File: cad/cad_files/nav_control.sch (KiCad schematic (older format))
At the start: 10 parts

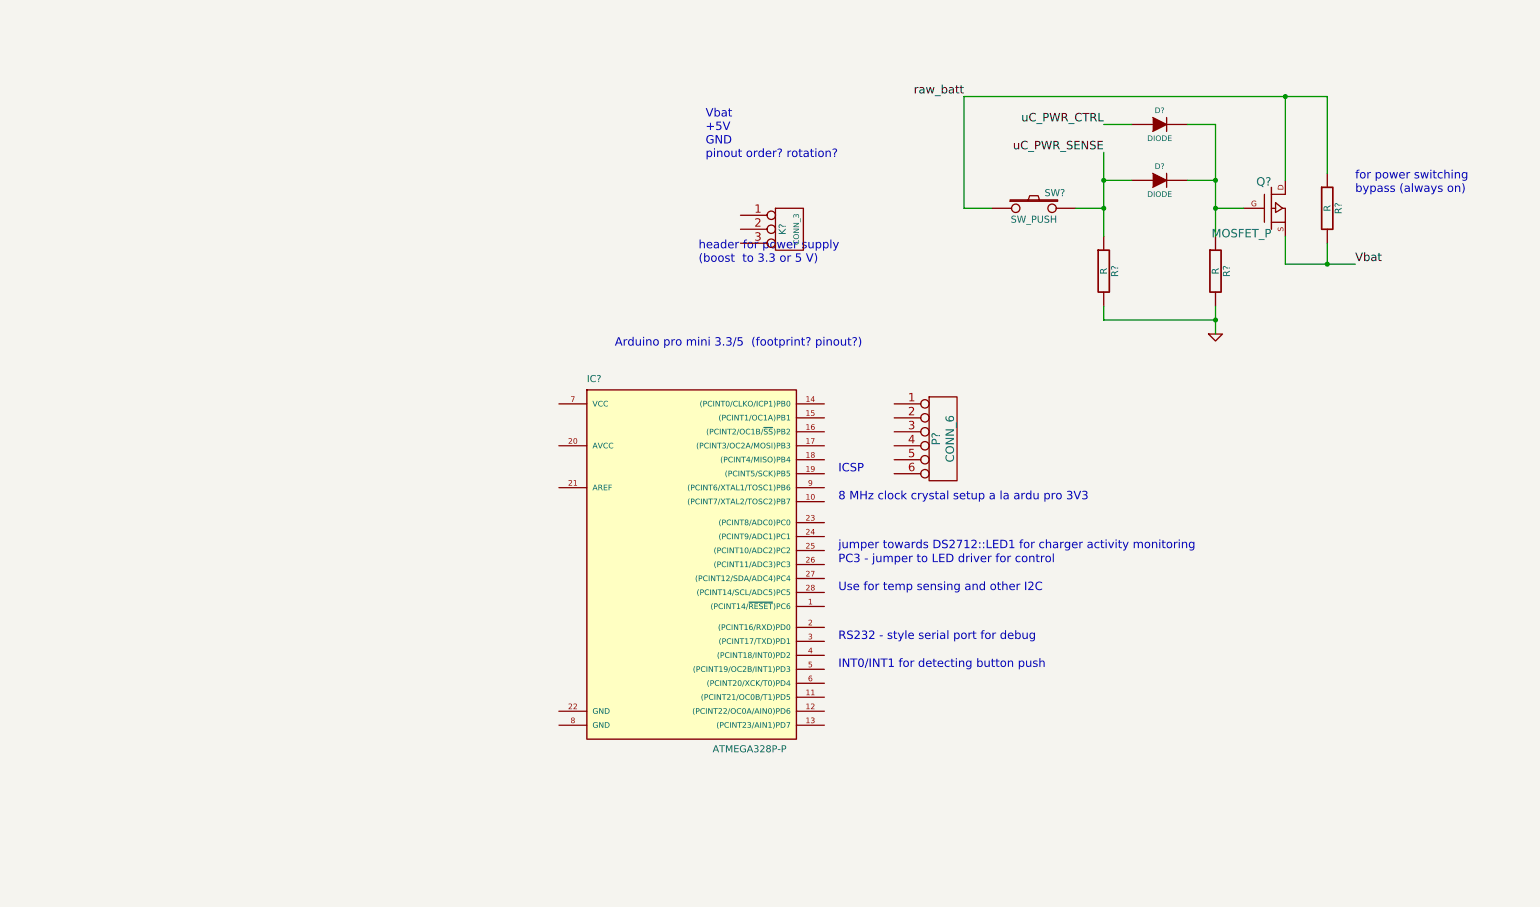
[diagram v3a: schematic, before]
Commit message: Arrange power and control connections
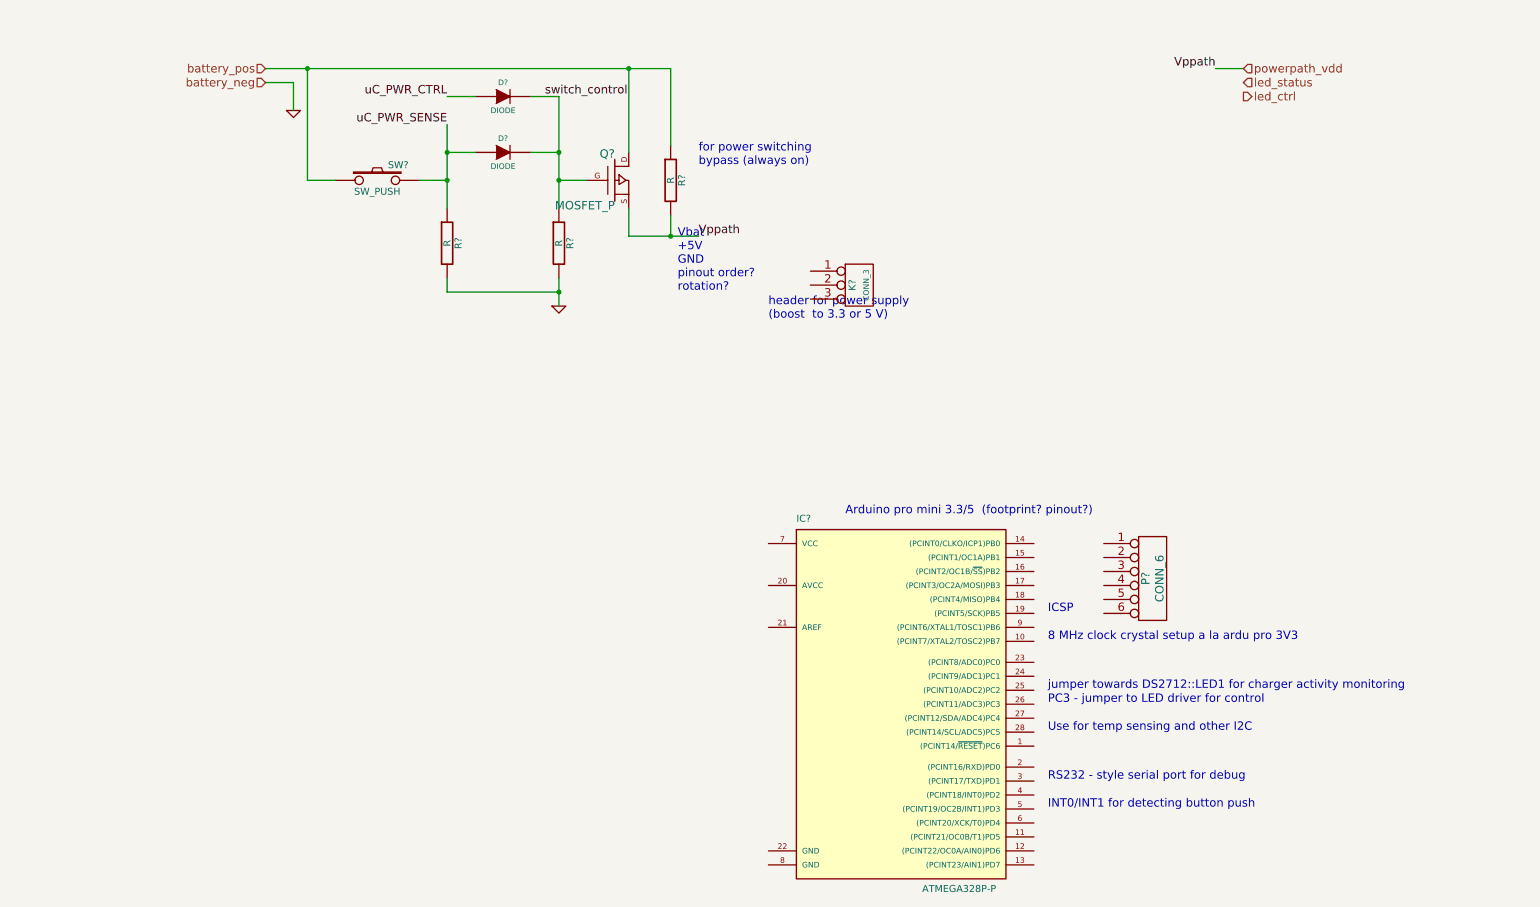
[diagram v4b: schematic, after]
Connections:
- net switch_control: now reaches D?.2 (K), D?.2 (K), Q?.G, R?.1
- net Vbat renamed powerpath_vdd
- net raw_batt renamed battery_pos
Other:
- note added: "Vbat\n+5V\nGND\npinout order? \nrotation?"
- note removed: "Vbat\n+5V\nGND\npinout order? rotation?"
- moved on the sheet: D?, IC?, K?, P?, Q?, R?, SW?
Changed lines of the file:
@@
-EESchema Schematic File Version 2  date Mon 01 Dec 2014 02:47:20 AM HST
+EESchema Schematic File Version 2  date Tue 02 Dec 2014 02:12:38 AM HST
 LIBS:local_parts
 LIBS:power
@@
 $Descr A4 11700 8267
 encoding utf-8
-Sheet 3 5
+Sheet 2 4
 Title ""
-Date "1 dec 2014"
+Date "2 dec 2014"
 Rev ""
 Comp ""
@@
 Comment4 ""
 $EndDescr
-Text Notes 4500 3000 0    60   ~ 0
+Text Label 4000 1200 0    60   ~ 0
+switch_control
+Wire Wire Line
+	9000 1000 8800 1000
+Connection ~ 2300 1000
+Wire Wire Line
+	2000 1000 4900 1000
+Connection ~ 4900 2200
+Wire Wire Line
+	4900 2050 4900 2200
+Wire Wire Line
+	4100 2700 4100 2500
+Wire Wire Line
+	2500 1800 2300 1800
+Wire Wire Line
+	2300 1800 2300 1000
+Connection ~ 4100 1800
+Wire Wire Line
+	4100 1800 4300 1800
+Wire Wire Line
+	3300 1200 3500 1200
+Connection ~ 3300 1600
+Wire Wire Line
+	3300 1600 3500 1600
+Wire Wire Line
+	3300 2000 3300 1400
+Wire Wire Line
+	3100 1800 3300 1800
+Connection ~ 3300 1800
+Wire Wire Line
+	3900 1600 4100 1600
+Wire Wire Line
+	3900 1200 4100 1200
+Wire Wire Line
+	4100 1200 4100 2000
+Connection ~ 4100 1600
+Wire Wire Line
+	5100 2200 4600 2200
+Wire Wire Line
+	4600 2200 4600 2000
+Wire Wire Line
+	4600 1000 4600 1600
+Wire Wire Line
+	3300 2500 3300 2600
+Wire Wire Line
+	3300 2600 4100 2600
+Connection ~ 4100 2600
+Wire Wire Line
+	4900 1000 4900 1550
+Connection ~ 4600 1000
+Wire Wire Line
+	2000 1100 2200 1100
+Wire Wire Line
+	2200 1100 2200 1300
+Text Label 8800 1000 2    60   ~ 0
+Vppath
+$Comp
+L GND #PWR?
+U 1 1 547DAB88
+P 2200 1300
+F 0 "#PWR?" H 2200 1300 30  0001 C CNN
+F 1 "GND" H 2200 1230 30  0001 C CNN
+	1    2200 1300
+	1    0    0    -1
+$EndComp
+Text HLabel 9000 1000 2    60   Input ~ 0
+powerpath_vdd
+Text HLabel 9000 1100 2    60   Input ~ 0
+led_status
+Text HLabel 9000 1200 2    60   Output ~ 0
+led_ctrl
+Text HLabel 2000 1100 0    60   Input ~ 0
+battery_neg
+Text HLabel 2000 1000 0    60   Input ~ 0
+battery_pos
+Text Notes 6150 4200 0    60   ~ 0
 Arduino pro mini 3.3/5  (footprint? pinout?)
-Text Notes 5150 1650 0    60   ~ 0
-Vbat\n+5V\nGND\npinout order? rotation?
-Text Notes 9800 1900 0    60   ~ 0
+Text Notes 4950 2600 0    60   ~ 0
+Vbat\n+5V\nGND\npinout order? \nrotation?
+Text Notes 5100 1700 0    60   ~ 0
 for power switching \nbypass (always on)
-Connection ~ 9300 1200
-Wire Wire Line
-	9600 1200 7000 1200
-Wire Wire Line
-	9600 1200 9600 1750
-Connection ~ 8800 2800
-Wire Wire Line
-	8800 2800 8000 2800
-Wire Wire Line
-	8000 2800 8000 2700
-Wire Wire Line
-	9300 1200 9300 1800
-Wire Wire Line
-	9300 2200 9300 2400
-Wire Wire Line
-	9300 2400 9800 2400
-Connection ~ 8800 1800
-Wire Wire Line
-	8800 2200 8800 1400
-Wire Wire Line
-	8800 1400 8600 1400
-Wire Wire Line
-	8600 1800 8800 1800
-Connection ~ 8000 2000
-Wire Wire Line
-	7800 2000 8000 2000
-Wire Wire Line
-	8000 2200 8000 1600
-Wire Wire Line
-	8000 1800 8200 1800
-Connection ~ 8000 1800
-Wire Wire Line
-	8000 1400 8200 1400
-Wire Wire Line
-	8800 2000 9000 2000
-Connection ~ 8800 2000
-Wire Wire Line
-	7000 1200 7000 2000
-Wire Wire Line
-	7000 2000 7200 2000
-Wire Wire Line
-	8800 2900 8800 2700
-Wire Wire Line
-	9600 2250 9600 2400
-Connection ~ 9600 2400
 $Comp
 L R R?
 U 1 1 547C6270
-P 9600 2000
-F 0 "R?" V 9680 2000 50  0000 C CNN
-F 1 "R" V 9600 2000 50  0000 C CNN
-	1    9600 2000
-	1    0    0    -1
-$EndComp
-Text Notes 5100 2400 0    60   ~ 0
+P 4900 1800
+F 0 "R?" V 4980 1800 50  0000 C CNN
+F 1 "R" V 4900 1800 50  0000 C CNN
+	1    4900 1800
+	1    0    0    -1
+$EndComp
+Text Notes 5600 2800 0    60   ~ 0
 header for power supply \n(boost  to 3.3 or 5 V)
 $Comp
 L CONN_3 K?
 U 1 1 546DDB52
-P 5750 2150
-F 0 "K?" V 5700 2150 50  0000 C CNN
-F 1 "CONN_3" V 5800 2150 40  0000 C CNN
-	1    5750 2150
-	1    0    0    -1
-$EndComp
-Text Notes 6100 4450 0    60   ~ 0
+P 6250 2550
+F 0 "K?" V 6200 2550 50  0000 C CNN
+F 1 "CONN_3" V 6300 2550 40  0000 C CNN
+	1    6250 2550
+	1    0    0    -1
+$EndComp
+Text Notes 7600 5450 0    60   ~ 0
 jumper towards DS2712::LED1 for charger activity monitoring
-Text Notes 6100 4550 0    60   ~ 0
+Text Notes 7600 5550 0    60   ~ 0
 PC3 - jumper to LED driver for control
-Text Notes 6100 4750 0    60   ~ 0
+Text Notes 7600 5750 0    60   ~ 0
 Use for temp sensing and other I2C
-Text Notes 6100 5300 0    60   ~ 0
+Text Notes 7600 6300 0    60   ~ 0
 INT0/INT1 for detecting button push
-Text Notes 6100 5100 0    60   ~ 0
+Text Notes 7600 6100 0    60   ~ 0
 RS232 - style serial port for debug
-Text Notes 6100 3900 0    60   ~ 0
+Text Notes 7600 4900 0    60   ~ 0
 ICSP
-Text Notes 6100 4100 0    60   ~ 0
+Text Notes 7600 5100 0    60   ~ 0
 8 MHz clock crystal setup a la ardu pro 3V3
 $Comp
 L CONN_6 P?
 U 1 1 53DE4465
-P 6850 3650
-F 0 "P?" V 6800 3650 60  0000 C CNN
-F 1 "CONN_6" V 6900 3650 60  0000 C CNN
-	1    6850 3650
+P 8350 4650
+F 0 "P?" V 8300 4650 60  0000 C CNN
+F 1 "CONN_6" V 8400 4650 60  0000 C CNN
+	1    8350 4650
 	1    0    0    -1
 $EndComp
@@
 L ATMEGA328P-P IC?
 U 1 1 53DE42CE
-P 5000 4500
-F 0 "IC?" H 4300 5750 50  0000 L BNN
-F 1 "ATMEGA328P-P" H 5200 3100 50  0000 L BNN
-F 2 "DIL28" H 4400 3150 50  0001 C CNN
-	1    5000 4500
+P 6500 5500
+F 0 "IC?" H 5800 6750 50  0000 L BNN
+F 1 "ATMEGA328P-P" H 6700 4100 50  0000 L BNN
+F 2 "DIL28" H 5900 4150 50  0001 C CNN
+	1    6500 5500
 	1    0    0    -1
 $EndComp
@@
 L GND #PWR?
 U 1 1 53DB8078
-P 8800 2900
-F 0 "#PWR?" H 8800 2900 30  0001 C CNN
-F 1 "GND" H 8800 2830 30  0001 C CNN
-	1    8800 2900
-	1    0    0    -1
-$EndComp
-Text Label 7000 1200 2    60   ~ 0
-raw_batt
-Text Label 8000 1600 2    60   ~ 0
+P 4100 2700
+F 0 "#PWR?" H 4100 2700 30  0001 C CNN
+F 1 "GND" H 4100 2630 30  0001 C CNN
+	1    4100 2700
+	1    0    0    -1
+$EndComp
+Text Label 3300 1400 2    60   ~ 0
 uC_PWR_SENSE
-Text Label 8000 1400 2    60   ~ 0
+Text Label 3300 1200 2    60   ~ 0
 uC_PWR_CTRL
-Text Label 9800 2400 0    60   ~ 0
-Vbat
+Text Label 5100 2200 0    60   ~ 0
+Vppath
 $Comp
 L MOSFET_P Q?
 U 1 1 53D1B1AA
-P 9200 2000
-F 0 "Q?" H 9200 2190 60  0000 R CNN
-F 1 "MOSFET_P" H 9200 1820 60  0000 R CNN
-	1    9200 2000
+P 4500 1800
+F 0 "Q?" H 4500 1990 60  0000 R CNN
+F 1 "MOSFET_P" H 4500 1620 60  0000 R CNN
+	1    4500 1800
 	1    0    0    -1
 $EndComp
@@
 L DIODE D?
 U 1 1 53D1B1A5
-P 8400 1400
-F 0 "D?" H 8400 1500 40  0000 C CNN
-F 1 "DIODE" H 8400 1300 40  0000 C CNN
-	1    8400 1400
+P 3700 1200
+F 0 "D?" H 3700 1300 40  0000 C CNN
+F 1 "DIODE" H 3700 1100 40  0000 C CNN
+	1    3700 1200
 	1    0    0    -1
 $EndComp
@@
 L DIODE D?
 U 1 1 53D1B19F
-P 8400 1800
-F 0 "D?" H 8400 1900 40  0000 C CNN
-F 1 "DIODE" H 8400 1700 40  0000 C CNN
-	1    8400 1800
+P 3700 1600
+F 0 "D?" H 3700 1700 40  0000 C CNN
+F 1 "DIODE" H 3700 1500 40  0000 C CNN
+	1    3700 1600
 	1    0    0    -1
 $EndComp
@@
 L R R?
 U 1 1 53D1B197
-P 8800 2450
-F 0 "R?" V 8880 2450 50  0000 C CNN
-F 1 "R" V 8800 2450 50  0000 C CNN
-	1    8800 2450
+P 4100 2250
+F 0 "R?" V 4180 2250 50  0000 C CNN
+F 1 "R" V 4100 2250 50  0000 C CNN
+	1    4100 2250
 	1    0    0    -1
 $EndComp
@@
 L R R?
 U 1 1 53D1B192
-P 8000 2450
-F 0 "R?" V 8080 2450 50  0000 C CNN
-F 1 "R" V 8000 2450 50  0000 C CNN
-	1    8000 2450
+P 3300 2250
+F 0 "R?" V 3380 2250 50  0000 C CNN
+F 1 "R" V 3300 2250 50  0000 C CNN
+	1    3300 2250
 	1    0    0    -1
 $EndComp
@@
 L SW_PUSH SW?
 U 1 1 53D1B188
-P 7500 2000
-F 0 "SW?" H 7650 2110 50  0000 C CNN
-F 1 "SW_PUSH" H 7500 1920 50  0000 C CNN
-	1    7500 2000
-	1    0    0    -1
-$EndComp
+P 2800 1800
+F 0 "SW?" H 2950 1910 50  0000 C CNN
+F 1 "SW_PUSH" H 2800 1720 50  0000 C CNN
+	1    2800 1800
+	1    0    0    -1
+$EndComp

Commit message: Add Arduino Pro Mini for control
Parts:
- added R?: R, symbol R
- added U?: ARDUINO_PRO_MINI, MODULE, symbol ARDUINO_PRO_MINI
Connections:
- net labels added: +5V
- wire segments 22 -> 30
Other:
- note added: "Vbat\n+5V\nGND"
- note added: "header for power supply \n(boost to 3.3 or 5 V)\ncheck rotation..."
- note removed: "Vbat\n+5V\nGND\npinout order? \nrotation?"
- note removed: "header for power supply \n(boost to 3.3 or 5 V)"
- moved on the sheet: K?
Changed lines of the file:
@@
-EESchema Schematic File Version 2  date Tue 02 Dec 2014 02:12:38 AM HST
+EESchema Schematic File Version 2  date Tue 02 Dec 2014 06:44:52 PM HST
 LIBS:local_parts
 LIBS:power
@@
 Sheet 2 4
 Title ""
-Date "2 dec 2014"
+Date "3 dec 2014"
 Rev ""
 Comp ""
@@
 Comment4 ""
 $EndDescr
+$Comp
+L R R?
+U 1 1 547E9539
+P 3900 4150
+F 0 "R?" V 3980 4150 50  0000 C CNN
+F 1 "R" V 3900 4150 50  0000 C CNN
+	1    3900 4150
+	1    0    0    -1
+$EndComp
+Wire Wire Line
+	4250 4250 4250 4750
+Wire Wire Line
+	4250 4750 3750 4750
+Wire Wire Line
+	5800 2500 5500 2500
+Wire Wire Line
+	5500 2500 5500 2400
+Wire Wire Line
+	9000 1000 8800 1000
+Connection ~ 2300 1000
+Wire Wire Line
+	2000 1000 4900 1000
+Connection ~ 4900 2200
+Wire Wire Line
+	4900 2050 4900 2200
+Wire Wire Line
+	4100 2700 4100 2500
+Wire Wire Line
+	2500 1800 2300 1800
+Wire Wire Line
+	2300 1800 2300 1000
+Connection ~ 4100 1800
+Wire Wire Line
+	4100 1800 4300 1800
+Wire Wire Line
+	3300 1200 3500 1200
+Connection ~ 3300 1600
+Wire Wire Line
+	3300 1600 3500 1600
+Wire Wire Line
+	3300 2000 3300 1400
+Wire Wire Line
+	3100 1800 3300 1800
+Connection ~ 3300 1800
+Wire Wire Line
+	3900 1600 4100 1600
+Wire Wire Line
+	3900 1200 4100 1200
+Wire Wire Line
+	4100 1200 4100 2000
+Connection ~ 4100 1600
+Wire Wire Line
+	4600 2000 4600 2200
+Wire Wire Line
+	4600 1000 4600 1600
+Wire Wire Line
+	3300 2500 3300 2600
+Wire Wire Line
+	3300 2600 4100 2600
+Connection ~ 4100 2600
+Wire Wire Line
+	4900 1000 4900 1550
+Connection ~ 4600 1000
+Wire Wire Line
+	2000 1100 2200 1100
+Wire Wire Line
+	2200 1100 2200 1300
+Wire Wire Line
+	4600 2200 5700 2200
+Wire Wire Line
+	5700 2200 5700 2400
+Wire Wire Line
+	5700 2400 5800 2400
+Wire Wire Line
+	5800 2600 5700 2600
+Wire Wire Line
+	5700 2600 5700 2700
+$Comp
+L +5V #PWR?
+U 1 1 547E94E8
+P 4250 4250
+F 0 "#PWR?" H 4250 4340 20  0001 C CNN
+F 1 "+5V" H 4250 4340 30  0000 C CNN
+	1    4250 4250
+	1    0    0    -1
+$EndComp
+$Comp
+L ARDUINO_PRO_MINI U?
+U 1 1 547E94C0
+P 3000 5000
+F 0 "U?" H 3000 4900 50  0000 C CNN
+F 1 "ARDUINO_PRO_MINI" H 3000 5650 50  0000 C CNN
+F 2 "MODULE" H 3000 5000 50  0001 C CNN
+F 3 "DOCUMENTATION" H 3000 5000 50  0001 C CNN
+	1    3000 5000
+	1    0    0    -1
+$EndComp
+$Comp
+L +5V #PWR?
+U 1 1 547E62DF
+P 5500 2400
+F 0 "#PWR?" H 5500 2490 20  0001 C CNN
+F 1 "+5V" H 5500 2490 30  0000 C CNN
+	1    5500 2400
+	1    0    0    -1
+$EndComp
+$Comp
+L GND #PWR?
+U 1 1 547E62B9
+P 5700 2700
+F 0 "#PWR?" H 5700 2700 30  0001 C CNN
+F 1 "GND" H 5700 2630 30  0001 C CNN
+	1    5700 2700
+	1    0    0    -1
+$EndComp
 Text Label 4000 1200 0    60   ~ 0
 switch_control
-Wire Wire Line
-	9000 1000 8800 1000
-Connection ~ 2300 1000
-Wire Wire Line
-	2000 1000 4900 1000
-Connection ~ 4900 2200
-Wire Wire Line
-	4900 2050 4900 2200
-Wire Wire Line
-	4100 2700 4100 2500
-Wire Wire Line
-	2500 1800 2300 1800
-Wire Wire Line
-	2300 1800 2300 1000
-Connection ~ 4100 1800
-Wire Wire Line
-	4100 1800 4300 1800
-Wire Wire Line
-	3300 1200 3500 1200
-Connection ~ 3300 1600
-Wire Wire Line
-	3300 1600 3500 1600
-Wire Wire Line
-	3300 2000 3300 1400
-Wire Wire Line
-	3100 1800 3300 1800
-Connection ~ 3300 1800
-Wire Wire Line
-	3900 1600 4100 1600
-Wire Wire Line
-	3900 1200 4100 1200
-Wire Wire Line
-	4100 1200 4100 2000
-Connection ~ 4100 1600
-Wire Wire Line
-	5100 2200 4600 2200
-Wire Wire Line
-	4600 2200 4600 2000
-Wire Wire Line
-	4600 1000 4600 1600
-Wire Wire Line
-	3300 2500 3300 2600
-Wire Wire Line
-	3300 2600 4100 2600
-Connection ~ 4100 2600
-Wire Wire Line
-	4900 1000 4900 1550
-Connection ~ 4600 1000
-Wire Wire Line
-	2000 1100 2200 1100
-Wire Wire Line
-	2200 1100 2200 1300
 Text Label 8800 1000 2    60   ~ 0
 Vppath
@@
 Text Notes 6150 4200 0    60   ~ 0
 Arduino pro mini 3.3/5  (footprint? pinout?)
-Text Notes 4950 2600 0    60   ~ 0
-Vbat\n+5V\nGND\npinout order? \nrotation?
+Text Notes 6300 2450 0    60   ~ 0
+Vbat\n+5V\nGND
 Text Notes 5100 1700 0    60   ~ 0
 for power switching \nbypass (always on)
@@
 	1    0    0    -1
 $EndComp
-Text Notes 5600 2800 0    60   ~ 0
-header for power supply \n(boost  to 3.3 or 5 V)
+Text Notes 5800 2800 0    60   ~ 0
+header for power supply \n(boost  to 3.3 or 5 V)\ncheck rotation...
 $Comp
 L CONN_3 K?
 U 1 1 546DDB52
-P 6250 2550
-F 0 "K?" V 6200 2550 50  0000 C CNN
-F 1 "CONN_3" V 6300 2550 40  0000 C CNN
-	1    6250 2550
-	1    0    0    -1
-$EndComp
+P 6150 2500
+F 0 "K?" V 6100 2500 50  0000 C CNN
+F 1 "CONN_3" V 6200 2500 40  0000 C CNN
+	1    6150 2500
+	1    0    0    -1
+$EndComp
